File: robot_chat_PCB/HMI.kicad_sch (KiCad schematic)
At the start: 17 parts, among them J501 Conn_01x06, SW201 SW_Push

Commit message: Mise à jour placement
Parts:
- D601: value LED_Small -> Border_Detect
- D602: value LED_Small -> Status
- D603: value LED_Small -> Error
- D604: value LED_Small -> Debug_1
- D605: value LED_Small -> Debug_2
- J501: value Conn_01x06 -> BT; footprint Connector_JST:JST_XH_S6B-XH-A_1x06_P2.50mm_Horizontal -> Connector_PinSocket_2.54mm:PinSocket_1x06_P2.54mm_Horizontal
- SW201: value SW_Push -> Start
- SW201: value SW_Push -> Status
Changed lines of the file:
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@@
   )
   (symbol (lib_id "Device:LED_Small") (at 86.36 129.54 180) (unit 1)
-    (in_bom yes) (on_board yes) (dnp no) (fields_autoplaced)
+    (in_bom yes) (on_board yes) (dnp no)
     (property "Reference" "D602" (at 86.2965 123.19 0)
-      (effects (font (size 1.27 1.27)))
-    )
-    (property "Value" "LED_Small" (at 86.2965 125.73 0)
+      (effects (font (size 1.27 1.27)) hide)
+    )
+    (property "Value" "Status" (at 87.63 127 0)
       (effects (font (size 1.27 1.27)))
     )
@@
     (in_bom yes) (on_board yes) (dnp no) (fields_autoplaced)
     (property "Reference" "SW201" (at 162.56 35.56 0)
-      (effects (font (size 1.27 1.27)))
-    )
-    (property "Value" "SW_Push" (at 162.56 38.1 0)
+      (effects (font (size 1.27 1.27)) hide)
+    )
+    (property "Value" "Start" (at 162.56 38.1 0)
       (effects (font (size 1.27 1.27)))
     )
@@
   )
   (symbol (lib_id "Device:LED_Small") (at 86.36 151.13 180) (unit 1)
-    (in_bom yes) (on_board yes) (dnp no) (fields_autoplaced)
+    (in_bom yes) (on_board yes) (dnp no)
     (property "Reference" "D604" (at 86.2965 144.78 0)
-      (effects (font (size 1.27 1.27)))
-    )
-    (property "Value" "LED_Small" (at 86.2965 147.32 0)
+      (effects (font (size 1.27 1.27)) hide)
+    )
+    (property "Value" "Debug_1" (at 87.63 148.59 0)
       (effects (font (size 1.27 1.27)))
     )
@@
     (in_bom yes) (on_board yes) (dnp no) (fields_autoplaced)
     (property "Reference" "SW201" (at 86.36 36.83 0)
-      (effects (font (size 1.27 1.27)))
-    )
-    (property "Value" "SW_Push" (at 86.36 39.37 0)
+      (effects (font (size 1.27 1.27)) hide)
+    )
+    (property "Value" "Status" (at 86.36 39.37 0)
       (effects (font (size 1.27 1.27)))
     )
@@
   )
   (symbol (lib_id "Device:LED_Small") (at 86.36 119.38 180) (unit 1)
-    (in_bom yes) (on_board yes) (dnp no) (fields_autoplaced)
+    (in_bom yes) (on_board yes) (dnp no)
     (property "Reference" "D601" (at 86.2965 113.03 0)
-      (effects (font (size 1.27 1.27)))
-    )
-    (property "Value" "LED_Small" (at 86.2965 115.57 0)
+      (effects (font (size 1.27 1.27)) hide)
+    )
+    (property "Value" "Border_Detect" (at 88.9 116.84 0)
       (effects (font (size 1.27 1.27)))
     )
@@
   )
   (symbol (lib_id "Device:LED_Small") (at 86.36 140.97 180) (unit 1)
-    (in_bom yes) (on_board yes) (dnp no) (fields_autoplaced)
+    (in_bom yes) (on_board yes) (dnp no)
     (property "Reference" "D603" (at 86.2965 134.62 0)
-      (effects (font (size 1.27 1.27)))
-    )
-    (property "Value" "LED_Small" (at 86.2965 137.16 0)
+      (effects (font (size 1.27 1.27)) hide)
+    )
+    (property "Value" "Error" (at 87.63 138.43 0)
       (effects (font (size 1.27 1.27)))
     )
@@
   )
   (symbol (lib_id "Device:LED_Small") (at 86.36 161.29 180) (unit 1)
-    (in_bom yes) (on_board yes) (dnp no) (fields_autoplaced)
+    (in_bom yes) (on_board yes) (dnp no)
     (property "Reference" "D605" (at 86.2965 154.94 0)
-      (effects (font (size 1.27 1.27)))
-    )
-    (property "Value" "LED_Small" (at 86.2965 157.48 0)
+      (effects (font (size 1.27 1.27)) hide)
+    )
+    (property "Value" "Debug_2" (at 87.63 158.75 0)
       (effects (font (size 1.27 1.27)))
     )
@@
     (in_bom yes) (on_board yes) (dnp no) (fields_autoplaced)
     (property "Reference" "J501" (at 237.49 45.72 0)
+      (effects (font (size 1.27 1.27)) (justify left) hide)
+    )
+    (property "Value" "BT" (at 237.49 48.26 0)
       (effects (font (size 1.27 1.27)) (justify left))
     )
-    (property "Value" "Conn_01x06" (at 237.49 48.26 0)
-      (effects (font (size 1.27 1.27)) (justify left))
-    )
-    (property "Footprint" "Connector_JST:JST_XH_S6B-XH-A_1x06_P2.50mm_Horizontal" (at 234.95 45.72 0)
-      (effects (font (size 1.27 1.27)) hide)
-    )
+    (property "Footprint" "Connector_PinSocket_2.54mm:PinSocket_1x06_P2.54mm_Horizontal" (at 234.95 45.72 0)
+      (effects (font (size 1.27 1.27)) hide)
+    )

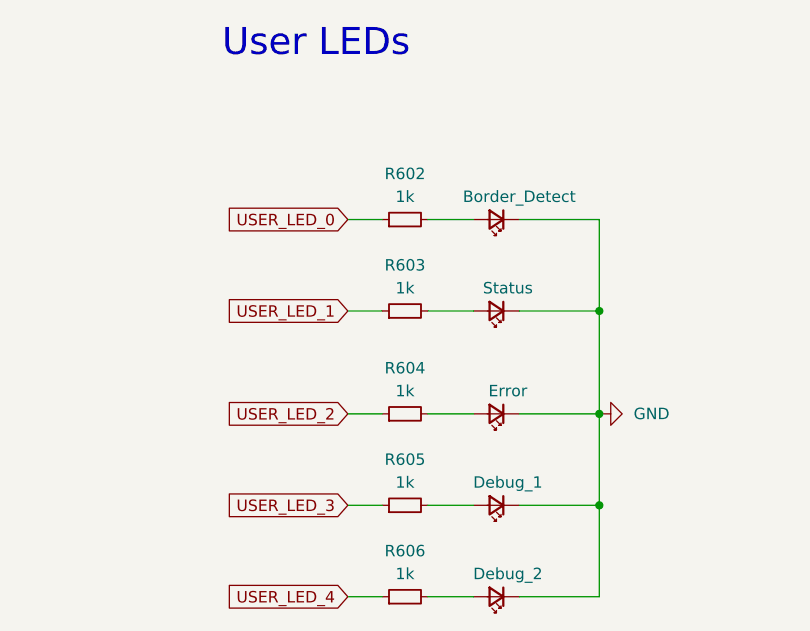
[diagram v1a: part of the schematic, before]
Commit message: changed Rsense position
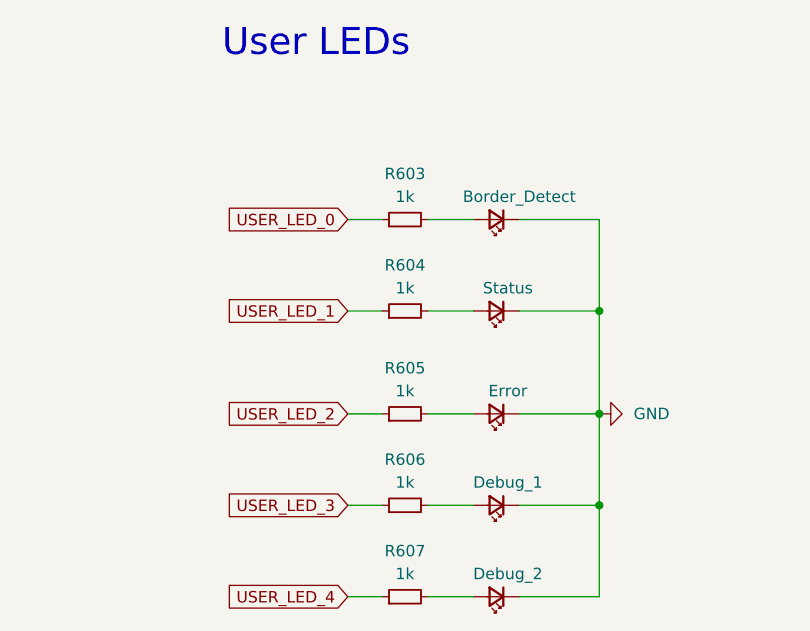
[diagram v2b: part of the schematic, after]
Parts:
- renumbered R602 to R603, R603 to R604, R604 to R605, R605 to R606, R606 to R607
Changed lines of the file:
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@@
         )
         (path "/74bedd9b-ffd1-4d8b-87e0-848eab324d95/441afe0d-0943-424c-9067-85108082b51d"
-          (reference "#PWR0604") (unit 1)
+          (reference "#PWR0605") (unit 1)
         )
       )
@@
   (symbol (lib_id "Device:R_Small") (at 76.2 151.13 90) (unit 1)
     (in_bom yes) (on_board yes) (dnp no) (fields_autoplaced)
-    (property "Reference" "R605" (at 76.2 146.05 90)
+    (property "Reference" "R606" (at 76.2 146.05 90)
       (effects (font (size 1.27 1.27)))
     )
@@
       (project "robot_chat"
         (path "/74bedd9b-ffd1-4d8b-87e0-848eab324d95/441afe0d-0943-424c-9067-85108082b51d"
-          (reference "R605") (unit 1)
+          (reference "R606") (unit 1)
         )
       )
@@
         )
         (path "/74bedd9b-ffd1-4d8b-87e0-848eab324d95/441afe0d-0943-424c-9067-85108082b51d"
-          (reference "R601") (unit 1)
+          (reference "R602") (unit 1)
         )
       )
@@
   (symbol (lib_id "Device:R_Small") (at 76.2 161.29 90) (unit 1)
     (in_bom yes) (on_board yes) (dnp no) (fields_autoplaced)
-    (property "Reference" "R606" (at 76.2 156.21 90)
+    (property "Reference" "R607" (at 76.2 156.21 90)
       (effects (font (size 1.27 1.27)))
     )
@@
       (project "robot_chat"
         (path "/74bedd9b-ffd1-4d8b-87e0-848eab324d95/441afe0d-0943-424c-9067-85108082b51d"
-          (reference "R606") (unit 1)
+          (reference "R607") (unit 1)
         )
       )
@@
         )
         (path "/74bedd9b-ffd1-4d8b-87e0-848eab324d95/441afe0d-0943-424c-9067-85108082b51d"
-          (reference "#PWR0606") (unit 1)
+          (reference "#PWR0602") (unit 1)
         )
       )
@@
         )
         (path "/74bedd9b-ffd1-4d8b-87e0-848eab324d95/441afe0d-0943-424c-9067-85108082b51d"
-          (reference "#PWR0605") (unit 1)
+          (reference "#PWR0601") (unit 1)
         )
       )
@@
         )
         (path "/74bedd9b-ffd1-4d8b-87e0-848eab324d95/441afe0d-0943-424c-9067-85108082b51d"
-          (reference "C601") (unit 1)
+          (reference "C602") (unit 1)
         )
       )
@@
         )
         (path "/74bedd9b-ffd1-4d8b-87e0-848eab324d95/441afe0d-0943-424c-9067-85108082b51d"
-          (reference "#PWR0601") (unit 1)
+          (reference "#PWR0606") (unit 1)
         )
       )
@@
         )
         (path "/74bedd9b-ffd1-4d8b-87e0-848eab324d95/441afe0d-0943-424c-9067-85108082b51d"
-          (reference "SW602") (unit 1)
+          (reference "SW601") (unit 1)
         )
       )
@@
   (symbol (lib_id "Device:R_Small") (at 76.2 129.54 90) (unit 1)
     (in_bom yes) (on_board yes) (dnp no) (fields_autoplaced)
-    (property "Reference" "R603" (at 76.2 124.46 90)
+    (property "Reference" "R604" (at 76.2 124.46 90)
       (effects (font (size 1.27 1.27)))
     )
@@
       (project "robot_chat"
         (path "/74bedd9b-ffd1-4d8b-87e0-848eab324d95/441afe0d-0943-424c-9067-85108082b51d"
-          (reference "R603") (unit 1)
+          (reference "R604") (unit 1)
         )
       )
@@
   (symbol (lib_id "power:GND") (at 97.79 140.97 90) (unit 1)
     (in_bom yes) (on_board yes) (dnp no) (fields_autoplaced)
-    (property "Reference" "#PWR0603" (at 104.14 140.97 0)
+    (property "Reference" "#PWR0607" (at 104.14 140.97 0)
       (effects (font (size 1.27 1.27)) hide)
     )
@@
       (project "robot_chat"
         (path "/74bedd9b-ffd1-4d8b-87e0-848eab324d95/441afe0d-0943-424c-9067-85108082b51d"
+          (reference "#PWR0607") (unit 1)
+        )
+      )
+    )
+  )
+  (symbol (lib_id "power:+3.3V") (at 96.52 44.45 0) (unit 1)
+    (in_bom yes) (on_board yes) (dnp no) (fields_autoplaced)
+    (property "Reference" "#PWR0202" (at 96.52 48.26 0)
+      (effects (font (size 1.27 1.27)) hide)
+    )
+    (property "Value" "+3.3V" (at 96.52 39.37 0)
+      (effects (font (size 1.27 1.27)))
+    )
+    (property "Footprint" "" (at 96.52 44.45 0)
+      (effects (font (size 1.27 1.27)) hide)
+    )
+    (property "Datasheet" "" (at 96.52 44.45 0)
+      (effects (font (size 1.27 1.27)) hide)
+    )
+    (pin "1")
+    (instances
+      (project "robot_chat"
+        (path "/74bedd9b-ffd1-4d8b-87e0-848eab324d95/40cef5c0-b6f0-48c1-9841-cd0790d0edde"
+          (reference "#PWR0202") (unit 1)
+        )
+        (path "/74bedd9b-ffd1-4d8b-87e0-848eab324d95/441afe0d-0943-424c-9067-85108082b51d"
           (reference "#PWR0603") (unit 1)
         )
@@
     )
   )
-  (symbol (lib_id "power:+3.3V") (at 96.52 44.45 0) (unit 1)
-    (in_bom yes) (on_board yes) (dnp no) (fields_autoplaced)
-    (property "Reference" "#PWR0202" (at 96.52 48.26 0)
-      (effects (font (size 1.27 1.27)) hide)
-    )
-    (property "Value" "+3.3V" (at 96.52 39.37 0)
-      (effects (font (size 1.27 1.27)))
-    )
-    (property "Footprint" "" (at 96.52 44.45 0)
-      (effects (font (size 1.27 1.27)) hide)
-    )
-    (property "Datasheet" "" (at 96.52 44.45 0)
-      (effects (font (size 1.27 1.27)) hide)
-    )
-    (pin "1")
-    (instances
-      (project "robot_chat"
-        (path "/74bedd9b-ffd1-4d8b-87e0-848eab324d95/40cef5c0-b6f0-48c1-9841-cd0790d0edde"
-          (reference "#PWR0202") (unit 1)
-        )
-        (path "/74bedd9b-ffd1-4d8b-87e0-848eab324d95/441afe0d-0943-424c-9067-85108082b51d"
-          (reference "#PWR0602") (unit 1)
-        )
-      )
-    )
-  )
   (symbol (lib_id "Device:R_Small") (at 76.2 119.38 90) (unit 1)
     (in_bom yes) (on_board yes) (dnp no) (fields_autoplaced)
-    (property "Reference" "R602" (at 76.2 114.3 90)
+    (property "Reference" "R603" (at 76.2 114.3 90)
       (effects (font (size 1.27 1.27)))
     )
@@
       (project "robot_chat"
         (path "/74bedd9b-ffd1-4d8b-87e0-848eab324d95/441afe0d-0943-424c-9067-85108082b51d"
-          (reference "R602") (unit 1)
+          (reference "R603") (unit 1)
         )
       )
@@
         )
         (path "/74bedd9b-ffd1-4d8b-87e0-848eab324d95/441afe0d-0943-424c-9067-85108082b51d"
-          (reference "SW601") (unit 1)
+          (reference "SW602") (unit 1)
         )
       )
@@
   (symbol (lib_id "Device:R_Small") (at 76.2 140.97 90) (unit 1)
     (in_bom yes) (on_board yes) (dnp no) (fields_autoplaced)
-    (property "Reference" "R604" (at 76.2 135.89 90)
+    (property "Reference" "R605" (at 76.2 135.89 90)
       (effects (font (size 1.27 1.27)))
     )
@@
       (project "robot_chat"
         (path "/74bedd9b-ffd1-4d8b-87e0-848eab324d95/441afe0d-0943-424c-9067-85108082b51d"
-          (reference "R604") (unit 1)
+          (reference "R605") (unit 1)
         )
       )
@@
         )
         (path "/74bedd9b-ffd1-4d8b-87e0-848eab324d95/441afe0d-0943-424c-9067-85108082b51d"
-          (reference "R607") (unit 1)
+          (reference "R601") (unit 1)
         )
       )
@@
         )
         (path "/74bedd9b-ffd1-4d8b-87e0-848eab324d95/441afe0d-0943-424c-9067-85108082b51d"
-          (reference "C602") (unit 1)
+          (reference "C601") (unit 1)
         )
       )
@@
         )
         (path "/74bedd9b-ffd1-4d8b-87e0-848eab324d95/441afe0d-0943-424c-9067-85108082b51d"
-          (reference "#PWR0607") (unit 1)
-        )
-      )
+          (reference "#PWR0604") (unit 1)
+        )
+      )

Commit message: fixed DRC, added html bom
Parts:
- D601, D603: Farnell Part Number (none) -> 3796316
- D602: Farnell Part Number (none) -> 3796304
- D604, D605: Farnell Part Number (none) -> 3796315
- J501: Farnell Part Number (none) -> 2827951
- SW201: Farnell Part Number (none) -> 1333652
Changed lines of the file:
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@@
+      (effects (font (size 1.27 1.27)) hide)
+    )
+    (property "Farnell Part Number" "3796304" (at 86.36 129.54 0)
       (effects (font (size 1.27 1.27)) hide)
     )
@@
     )
     (property "Datasheet" "~" (at 162.56 38.1 0)
+      (effects (font (size 1.27 1.27)) hide)
+    )
+    (property "Farnell Part Number" "1333652" (at 162.56 43.18 0)
       (effects (font (size 1.27 1.27)) hide)
     )
@@
       (effects (font (size 1.27 1.27)) hide)
     )
+    (property "Farnell Part Number" "3796315" (at 86.36 151.13 0)
+      (effects (font (size 1.27 1.27)) hide)
+    )
     (pin "1")
     (pin "2")
@@
     )
     (property "Datasheet" "~" (at 86.36 39.37 0)
+      (effects (font (size 1.27 1.27)) hide)
+    )
+    (property "Farnell Part Number" "1333652" (at 86.36 44.45 0)
       (effects (font (size 1.27 1.27)) hide)
     )
@@
       (effects (font (size 1.27 1.27)) hide)
     )
+    (property "Farnell Part Number" "3796316" (at 86.36 119.38 0)
+      (effects (font (size 1.27 1.27)) hide)
+    )
     (pin "1")
     (pin "2")
@@
       (effects (font (size 1.27 1.27)) hide)
     )
+    (property "Farnell Part Number" "3796316" (at 86.36 140.97 0)
+      (effects (font (size 1.27 1.27)) hide)
+    )
     (pin "1")
     (pin "2")
@@
       (effects (font (size 1.27 1.27)) hide)
     )
+    (property "Farnell Part Number" "3796315" (at 86.36 161.29 0)
+      (effects (font (size 1.27 1.27)) hide)
+    )
     (pin "1")
     (pin "2")
@@
       (effects (font (size 1.27 1.27)) hide)
     )
+    (property "Farnell Part Number" "2827951" (at 234.95 45.72 0)
+      (effects (font (size 1.27 1.27)) hide)
+    )
